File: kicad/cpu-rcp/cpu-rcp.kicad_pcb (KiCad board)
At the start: 4 copper layers, 80 x 57.1 mm, 77 parts, among them P1 RDRAM-EDGE, P5 NINTENDO-64_PINHEAD-25X2, SW1 Reset, U10 CPU-NUS, U3 U3, U6 PIF-NUS, U7 MX8330, U8 LC125, U9 RCP-NUS, X1 14.318MHz

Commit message: Another rebuild, WIP
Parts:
- added R13: 4K3, n64:R_0603, F.Cu at (59.0, 67.2)
- C123, C127, C128, CVT1, DA1, R22, R23, R24, R28, R3, R34, R4, SW1: moved to F.Cu
- C144: value ± -> ~; footprint n64:C_0805 -> n64:C_0603
- C6, C7, C8, C9: footprint n64:C_0805 -> n64:C_0603
- CC1, CC2, CC3, CC4, CC5, CC6, CC7, CC8, CC9, CR1, CR10, CR11, CR12, CR13, CR14, CR15, CR2, CR3, CR4, CR5, CR6, CR7, CR8, CR9, CU1, CU6, CU7, CU8, CVR1, CVR2, CVT2: value 100nF -> .1uF; moved to F.Cu
- U3: footprint n64:sot-23-5 -> n64:u3-sot-23-5
- U6: footprint n64:so-28w -> n64:pif-nus-so-28w
- U7: footprint n64:so-8 -> n64:mx8330-sop-8
- U8: footprint n64:ssop-14 -> n64:u8-ssop-14
- moved JOY1 72.7 mm to (104.6, 33.9), turned to 270 degrees
- moved R37 71.5 mm to (100.6, 30.9), turned to 180 degrees
- moved R28 70.3 mm to (65.5, 93.6)
- moved FIL4 67.9 mm to (100.7, 35.8), turned to 0 degrees
- moved R34 67.9 mm to (65.2, 93.5)
- moved R23 67.7 mm to (66.2, 93.6)
- moved R22 67.0 mm to (65.6, 93.6)
- moved SW1 66.8 mm to (68.4, 93.8)
- moved FIL2 65.8 mm to (100.7, 33.0), turned to 0 degrees
- moved CU6 63.7 mm to (67.1, 92.9)
- moved R38 63.4 mm to (100.8, 37.8), turned to 180 degrees
- moved C123 60.7 mm to (65.9, 93.7), turned to 0 degrees
- moved CC1 60.5 mm to (67.7, 93.1)
- moved CU8 58.9 mm to (67.1, 92.9), turned to 0 degrees
- moved CR7 57.9 mm to (68.2, 93.3)
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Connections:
- C144 pad 1: GND -> ENABLE_CLK
- C144 pad 2: Net-(C144-Pad2) -> GND
- P1 pad 18: ENABLE -> ENABLE_CLK
- R36 pad 1: ENABLE -> ENABLE_CLK
- R36 pad 2: Net-(C144-Pad2) -> ENABLE
- U7 pad 7: Net-(C144-Pad2) -> ENABLE_CLK
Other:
- net class Default: clearance 0.15 -> 0.2; trace_width 0.15 -> 0.25; via_dia 0.3 -> 0.45; via_drill 0.2 -> 0.3
- net class PWR: trace_width 0.3 -> 0.37; via_dia 0.6 -> 0.5; via_drill 0.4 -> 0.3
- rule trace_clearance: 0.15 -> 0.2
- rule trace_min: 0.1 -> 0.2
- rule via_min_drill: 0.2 -> 0.3
- rule via_min_size: 0.2 -> 0.45

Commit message: WIP
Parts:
- added AVSYNC1: VIDEO ENCODER SYNC, n64:connector-molex-505110-0492, F.Cu at (65.4, 92.7)
- moved CC9 55.8 mm to (37.1, 47.3)
- moved CR7 55.8 mm to (36.8, 47.2)
- moved CU1 55.8 mm to (35.6, 46.8)
- moved R2 55.8 mm to (34.9, 47.6)
- moved R28 55.8 mm to (34.1, 47.5)
- moved C142 55.8 mm to (34.3, 47.6)
- moved C39 55.8 mm to (35.2, 46.6)
- moved C40 55.8 mm to (35.9, 46.9)
- moved CC2 55.8 mm to (36.4, 47.0)
- moved CC3 55.8 mm to (36.0, 46.9)
- moved CC6 55.8 mm to (36.7, 47.1)
- moved CC7 55.8 mm to (36.5, 47.1)
- moved CR14 55.8 mm to (37.2, 47.3)
- moved CR2 55.8 mm to (35.5, 46.7)
- moved CR4 55.8 mm to (37.4, 47.4)
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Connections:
- P5 pad 10: /CART_READ -> CART_ADDR07
- P5 pad 11: CART_ADDR11 -> CART_ADDR06
- P5 pad 12: CART_ADDR10 -> (no net)
- P5 pad 15: CART_ADDR09 -> CART_ADDR04
- P5 pad 16: CART_ADDR08 -> CART_ALE_H
- P5 pad 18: CIC_IN -> CART_ALE_L
- P5 pad 19: CIC_CLK -> CART_ADDR03
- P5 pad 2: GND -> (no net)
- P5 pad 20: /COLDRESET -> GND
- P5 pad 21: EEPROM_DAT -> CART_ADDR02
- P5 pad 22: GND -> CART_ADDR01
- P5 pad 23: GND -> CART_ADDR00
- P5 pad 24: (no net) -> GND
- P5 pad 27: GND -> (no net)
- P5 pad 28: CART_ADDR00 -> GND
- P5 pad 29: CART_ADDR01 -> GND
- P5 pad 3: CART_ADDR15 -> GND
- P5 pad 30: CART_ADDR02 -> EEPROM_DAT
- P5 pad 31: GND -> /COLDRESET
- P5 pad 32: CART_ADDR03 -> CIC_CLK
- P5 pad 33: CART_ALE_L -> CIC_IN
- P5 pad 35: CART_ALE_H -> CART_ADDR08
- P5 pad 36: CART_ADDR04 -> CART_ADDR09
- P5 pad 37: CART_ADDR05 -> (no net)
- P5 pad 4: CART_ADDR14 -> GND
- P5 pad 40: CART_ADDR06 -> CART_ADDR11
- P5 pad 41: CART_ADDR07 -> /CART_READ
- P5 pad 43: CIC_OUT -> /CART_WRITE
- P5 pad 44: JTCK -> CART_ADDR12
- P5 pad 45: /NMI -> GND
- P5 pad 46: /External connections/VIDEO_SYNC -> CART_ADDR13
- P5 pad 47: GND -> CART_ADDR14
- P5 pad 48: GND -> CART_ADDR15
- P5 pad 49: (no net) -> GND
- P5 pad 5: CART_ADDR13 -> /External connections/VIDEO_SYNC
- P5 pad 6: GND -> /NMI
- P5 pad 7: CART_ADDR12 -> JTCK
- P5 pad 8: /CART_WRITE -> CIC_OUT
- U9 pad 35: CART_ADDR05 -> (no net)
- U9 pad 38: CART_ADDR10 -> (no net)

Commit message: Better layout, work in progress
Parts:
- removed AVSYNC1: VIDEO ENCODER SYNC, n64:connector-molex-505110-0492
- added REF**: MountingHole_3.2mm_M3, Mounting_Holes:MountingHole_3.2mm_M3, F.Cu at (111.8, 29.2)
- C142, D2, DA1: moved to B.Cu
- P5: value NINTENDO-64_PINHEAD-25X2 -> 502790-5091
- moved C73 68.9 mm to (97.7, 74.9)
- moved D2 50.7 mm to (96.0, 45.7), turned to 90 degrees
- moved DCIN1 46.0 mm to (34.1, 31.6)
- moved U3 36.2 mm to (41.1, 34.8)
- moved C128 36.0 mm to (34.8, 35.2)
- moved DA1 35.7 mm to (65.7, 47.6), turned to 180 degrees
- moved R37 31.1 mm to (101.1, 62.0), turned to 90 degrees
- moved FIL2 26.7 mm to (101.0, 59.7)
- moved JOY1 23.6 mm to (105.0, 57.6)
- moved FIL4 21.6 mm to (101.0, 57.4)
- moved R38 17.0 mm to (101.0, 54.9), turned to 270 degrees
- moved P5 9.66 mm to (96.5, 29.9)
- moved U6 8.74 mm to (87.6, 47.1)
- moved U8 8.25 mm to (74.4, 50.9), turned to 0 degrees
- moved U7 8.00 mm to (62.6, 72.5)
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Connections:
- JOY1 pad 1: +3V3 -> GND
- JOY1 pad 2: Net-(FIL2-Pad2) -> Net-(FIL4-Pad2)
- JOY1 pad 3: Net-(FIL4-Pad2) -> Net-(FIL2-Pad2)
- JOY1 pad 4: GND -> +3V3
- P5 pad 10: CART_ADDR07 -> EEPROM_DAT
- P5 pad 11: CART_ADDR06 -> CIC_CLK
- P5 pad 12: (no net) -> CIC_OUT
- P5 pad 13: (no net) -> CIC_IN
- P5 pad 14: (no net) -> /COLDRESET
- P5 pad 15: CART_ADDR04 -> /NMI
- P5 pad 16: CART_ALE_H -> +3V3
- P5 pad 18: CART_ALE_L -> CART_ADDR07
- P5 pad 19: CART_ADDR03 -> CART_ADDR08
- P5 pad 2: (no net) -> GND
- P5 pad 20: GND -> CART_ADDR06
- P5 pad 21: CART_ADDR02 -> CART_ADDR09
- P5 pad 22: CART_ADDR01 -> GND
- P5 pad 23: CART_ADDR00 -> GND
- P5 pad 24: GND -> +3V3
- P5 pad 25: GND -> +3V3
- P5 pad 26: GND -> CART_ADDR05
- P5 pad 27: (no net) -> CART_ADDR10
- P5 pad 28: GND -> CART_ADDR04
- P5 pad 29: GND -> CART_ADDR11
- P5 pad 3: GND -> (no net)
- P5 pad 30: EEPROM_DAT -> CART_ALE_H
- P5 pad 31: /COLDRESET -> /CART_READ
- P5 pad 32: CIC_CLK -> +3V3
- P5 pad 33: CIC_IN -> +3V3
- P5 pad 34: +3V3 -> CART_ALE_L
- P5 pad 35: CART_ADDR08 -> /CART_WRITE
- P5 pad 36: CART_ADDR09 -> CART_ADDR03
- P5 pad 37: (no net) -> CART_ADDR12
- P5 pad 38: (no net) -> GND
- P5 pad 39: (no net) -> GND
- P5 pad 4: GND -> (no net)
- P5 pad 40: CART_ADDR11 -> CART_ADDR02
- P5 pad 41: /CART_READ -> CART_ADDR13
- P5 pad 42: +3V3 -> CART_ADDR01
- P5 pad 43: /CART_WRITE -> CART_ADDR14
- P5 pad 44: CART_ADDR12 -> CART_ADDR00
- P5 pad 45: GND -> CART_ADDR15
- P5 pad 46: CART_ADDR13 -> GND
- P5 pad 47: CART_ADDR14 -> GND
- P5 pad 48: CART_ADDR15 -> GND
- P5 pad 5: /External connections/VIDEO_SYNC -> GND
- P5 pad 50: GND -> JTCK
- P5 pad 6: /NMI -> GND
- P5 pad 7: JTCK -> GND
- P5 pad 8: CIC_OUT -> GND
- P5 pad 9: +3V3 -> /External connections/VIDEO_SYNC
- U9 pad 35: (no net) -> CART_ADDR05
- U9 pad 38: (no net) -> CART_ADDR10
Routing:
- net JOY2_DATA: track 0.00 -> 34.6 mm
- net JOY1_DATA: track 0.00 -> 32.9 mm
- net EEPROM_DAT: track 0.00 -> 32.7 mm, vias 0 -> 1
- net /NMI: track 0.00 -> 20.9 mm, vias 0 -> 1
- net /COLDRESET: track 0.00 -> 20.2 mm, vias 0 -> 1
- net CIC_IN: track 0.00 -> 18.7 mm, vias 0 -> 1
- net CIC_OUT: track 0.00 -> 16.0 mm, vias 0 -> 1
- net CART_ADDR14: track 0.00 -> 14.3 mm
- net PIF_CLK: track 0.00 -> 13.4 mm, vias 0 -> 1
- net Net-(U6-Pad18): track 0.00 -> 13.3 mm
- net CART_ADDR00: track 0.00 -> 12.9 mm
- net Net-(U6-Pad16): track 0.00 -> 12.2 mm
- net CART_ADDR15: track 0.00 -> 12.1 mm
- net CIC_CLK: track 0.00 -> 11.8 mm, vias 0 -> 1
- net PIF_ADR: track 0.00 -> 11.5 mm, vias 0 -> 1
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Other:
- board size 80 x 57.1 mm -> 90.2 x 57.1 mm
- net class PWR: clearance 0.3 -> 0.2; trace_width 0.37 -> 0.35

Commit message: WIP
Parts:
- C123, CU6, CU8: moved to B.Cu
- C142: moved to F.Cu
- moved CU6 48.1 mm to (82.8, 37.1)
- moved C123 42.9 mm to (77.9, 40.1), turned to 180 degrees
- moved CU8 38.6 mm to (74.4, 47.1), turned to 180 degrees
- moved DA1 27.4 mm to (90.8, 58.5)
- moved C142 22.6 mm to (41.6, 30.7), turned to 180 degrees
- moved C127 20.6 mm to (47.3, 31.5)
- moved R34 11.3 mm to (31.1, 36.4), turned to 270 degrees
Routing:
- net JOY2_DATA: track 34.6 -> 33.5 mm

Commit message: WIP
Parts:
- removed CU1: .1uF, n64:C_0603
- C127, C128, CC1, CC2, CC3, CC4, CC5, CC6, CC7, CC8, CC9, CR1, CR10, CR11, CR12, CR13, CR14, CR15, CR2, CR3, CR4, CR5, CR6, CR7, CR8, CR9, CU7, CVR1, CVR2, R22, R23, R3, R4, SW1: moved to B.Cu
- D2: moved to F.Cu
- moved C73 71.4 mm to (41.9, 30.4), turned to 90 degrees
- moved R28 68.2 mm to (102.1, 52.6)
- moved CVT2 66.6 mm to (96.1, 74.4)
- moved CVT1 66.5 mm to (96.4, 71.6)
- moved CR2 65.4 mm to (100.8, 47.0), turned to 270 degrees
- moved CR3 64.4 mm to (100.8, 41.1), turned to 270 degrees
- moved R3 63.2 mm to (96.8, 40.0)
- moved R4 62.9 mm to (96.8, 41.9)
- moved C128 62.8 mm to (97.5, 37.1), turned to 0 degrees
- moved CR1 59.9 mm to (95.2, 61.0), turned to 90 degrees
- moved CR15 57.9 mm to (92.6, 63.5)
- moved CR4 57.8 mm to (93.9, 34.8)
- moved CVR1 57.6 mm to (88.3, 74.4), turned to 270 degrees
- moved D2 55.4 mm to (41.8, 34.4)
- moved CR14 54.4 mm to (89.2, 63.6)
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
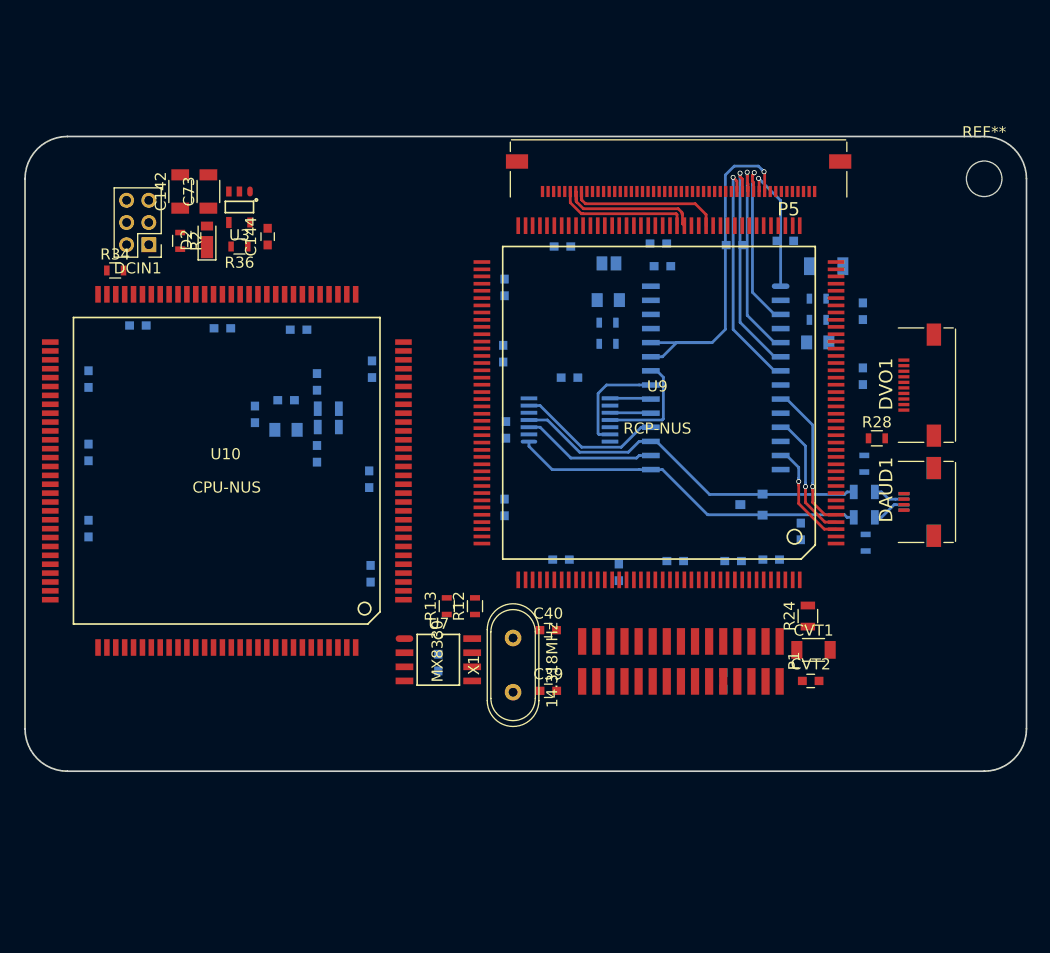
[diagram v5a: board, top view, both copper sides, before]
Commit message: Laying around, cleanier look
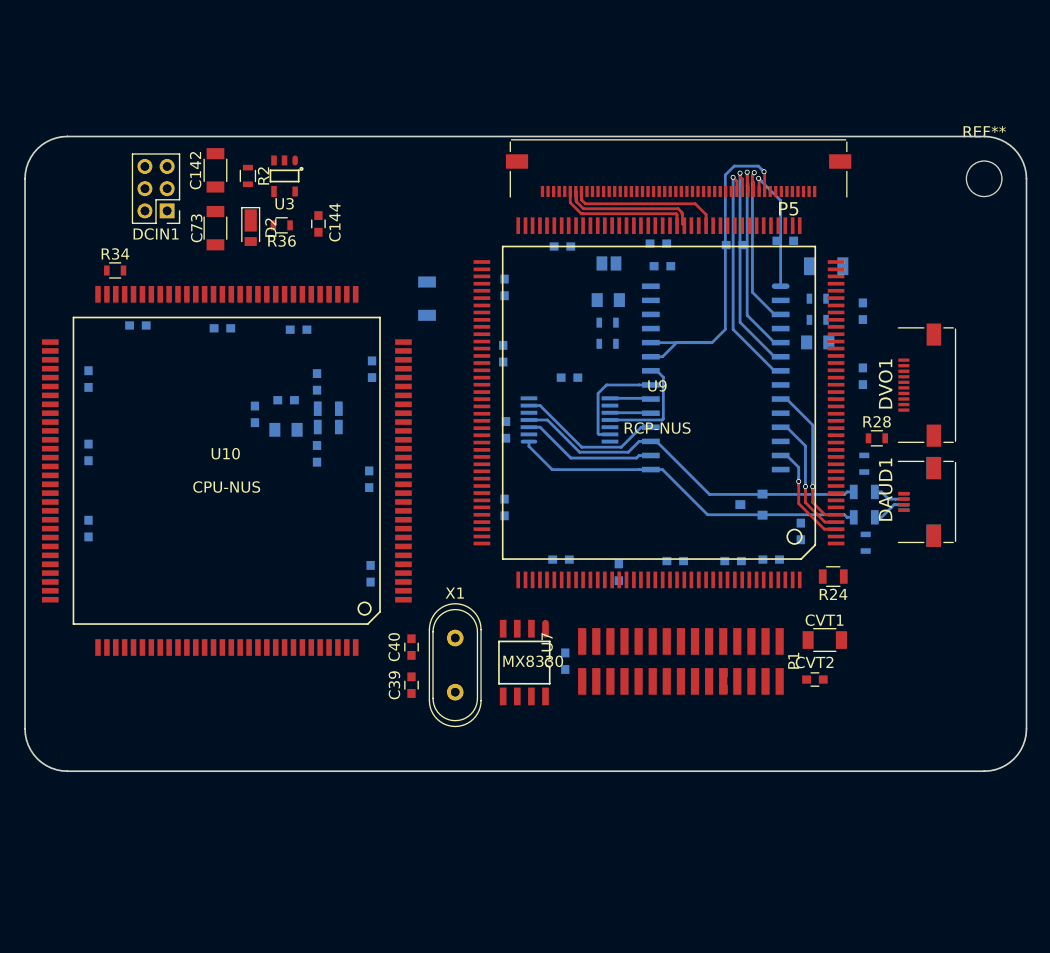
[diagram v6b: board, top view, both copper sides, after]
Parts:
- removed R12: 820R, n64:R_0603
- removed R13: 4K3, n64:R_0603
- added C134: 68uF, n64:C_1206, B.Cu at (61.6, 40.0)
- moved C40 12.4 mm to (60.2, 71.4), turned to 270 degrees
- moved C39 12.3 mm to (60.2, 74.8), turned to 90 degrees
- moved CU7 11.4 mm to (74.0, 72.6)
- moved R2 8.44 mm to (45.5, 29.0)
- moved U7 7.75 mm to (70.4, 72.8), turned to 270 degrees
- moved X1 5.21 mm to (64.1, 73.0)
- moved U3 4.93 mm to (48.8, 29.0)
- moved C144 4.71 mm to (51.8, 33.3), turned to 270 degrees
- moved R36 4.26 mm to (48.5, 33.4)
- moved R24 4.23 mm to (98.2, 65.0), turned to 180 degrees
- moved D2 3.97 mm to (45.7, 33.9), turned to 270 degrees
- moved C142 3.70 mm to (42.5, 28.4)
- moved DCIN1 3.47 mm to (38.2, 32.1)
- moved C73 3.36 mm to (42.5, 33.7), turned to 270 degrees
- moved CVT1 1.35 mm to (97.4, 70.7)
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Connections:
- P5 pad 3: (no net) -> Net-(P5-Pad3)
- P5 pad 4: (no net) -> Net-(P5-Pad4)
- U10 pad 18: (no net) -> Net-(U10-Pad18)
- U10 pad 65: (no net) -> Net-(U10-Pad65)
- U10 pad 74: (no net) -> Net-(U10-Pad74)
- U10 pad 95: (no net) -> Net-(U10-Pad95)
- U6 pad 26: (no net) -> Net-(U6-Pad26)
- U7 pad 3: (no net) -> Net-(U7-Pad3)

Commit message: Laying around
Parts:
- C142, C73, D2: moved to B.Cu
- moved D2 51.7 mm to (95.9, 46.5), turned to 90 degrees
- moved CR3 10.0 mm to (96.8, 50.3)
- moved CR2 9.66 mm to (96.8, 55.8)
- moved U3 7.90 mm to (41.5, 32.1), turned to 0 degrees
- moved C144 6.25 mm to (46.1, 30.7)
- moved R36 5.92 mm to (45.5, 28.3)
- moved R2 3.99 mm to (41.5, 28.3), turned to 0 degrees
- moved R34 3.94 mm to (29.6, 37.1)
- moved CR5 3.43 mm to (85.9, 35.1)
- moved U10 3.24 mm to (44.2, 52.3)
- moved C134 2.81 mm to (62.5, 42.7)
- moved C73 1.99 mm to (41.7, 31.9), turned to 0 degrees
- moved CR6 1.78 mm to (80.6, 35.1)
- moved CR1 1.65 mm to (96.8, 61.6)
- moved C142 1.27 mm to (41.5, 29.2), turned to 0 degrees
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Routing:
- net PIF_CLK: track 13.4 -> 18.9 mm
- net PIF_ADR: track 11.5 -> 16.2 mm
- net PIF_DAT: track 9.71 -> 12.8 mm
- net JOY2_DATA: track 33.5 -> 32.9 mm
- added copper zone on F.Cu, net GND

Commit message: WIP
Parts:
- added REF**: MountingHole_3.2mm_M3, Mounting_Holes:MountingHole_3.2mm_M3, F.Cu at (105.4, 78.7)
- D2: footprint n64:D_TUMD2 -> n64:D_0805
- DAUD1, JOY1: footprint n64:connector-molex-505110-0492 -> n64:Connectors_GS4
- DVO1: footprint n64:connector-molex-505110-1092 -> n64:Connectors_GS10
- moved REF** 82.6 mm to (29.2, 26.7)
- moved C73 46.2 mm to (40.5, 78.1)
- moved C142 46.2 mm to (40.4, 75.4)
- moved R2 46.0 mm to (39.6, 74.3)
- moved R36 45.8 mm to (43.1, 74.0)
- moved U3 45.6 mm to (39.6, 77.7)
- moved DCIN1 45.4 mm to (31.4, 77.6), turned to 90 degrees
- moved C144 43.3 mm to (46.5, 74.0), turned to 0 degrees
- moved R28 35.4 mm to (70.7, 69.0), turned to 90 degrees
- moved FIL2 10.3 mm to (96.1, 68.8)
- moved R37 10.3 mm to (96.1, 70.4)
- moved FIL4 10.3 mm to (96.1, 66.5)
- moved JOY1 10.3 mm to (100.2, 66.7)
- moved R38 10.3 mm to (96.1, 65.0)
- moved DVO1 6.47 mm to (100.5, 55.5)
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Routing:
- net /SYSAD28: track 0.00 -> 47.6 mm, vias 0 -> 2
- net /SYSAD27: track 0.00 -> 46.6 mm, vias 0 -> 2
- net /SYSAD26: track 0.00 -> 39.4 mm, vias 0 -> 2
- net Net-(DVO1-Pad2): track 0.00 -> 36.4 mm, vias 0 -> 2
- net /SYSAD25: track 0.00 -> 34.7 mm, vias 0 -> 2
- net JOY2_DATA: track 32.9 -> 0.00 mm
- net JOY1_DATA: track 32.9 -> 0.00 mm
- net EEPROM_DAT: track 32.7 -> 0.00 mm, vias 1 -> 0
- net ENABLE_CLK: track 0.00 -> 26.0 mm
- net /NMI: track 20.9 -> 0.00 mm, vias 1 -> 0
- net /COLDRESET: track 20.2 -> 0.00 mm, vias 1 -> 0
- net PIF_CLK: track 18.9 -> 0.00 mm, vias 1 -> 0
- net CIC_IN: track 18.7 -> 0.00 mm, vias 1 -> 0
- net PIF_ADR: track 16.2 -> 0.00 mm, vias 1 -> 0
- net CIC_OUT: track 16.0 -> 0.00 mm, vias 1 -> 0
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- added copper zone on B.Cu, net GND
- removed copper zone on F.Cu, net GND
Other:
- board size 90.2 x 57.1 mm -> 76.2 x 59.7 mm
